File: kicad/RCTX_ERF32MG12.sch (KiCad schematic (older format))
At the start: 87 parts

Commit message: Using ERF32FG12 SoC instead of PIC32MX
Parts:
- removed C? (x2): 10u, symbol device:C
- removed C?: 10n, symbol device:C
- removed C? (x6): 1u, symbol device:C
- removed C? (x4): 100n, symbol device:C
- removed C?: 10p, symbol device:C
- removed C?: 100p, symbol device:C
- removed C?: 4u7, symbol device:C
- removed L?: BLM18AG601SN1, symbol device:L_Core_Iron
- removed L?: 4u7, symbol device:L
- removed R?: 1R, symbol device:R
- removed U?: EFR32FG12P431F1024GM68, Footprint, symbol silabs_efr32:EFR32FG12P431F1024GM68
- added C? (x2): 3p, symbol device:C
- added C?: 47u, symbol device:C
- added C?: 82u, symbol device:C
- added C? (x2): 10p, symbol device:C
- added C?: 220n, symbol device:C
- added C? (x5): 100n, symbol device:C
- added C?: 4u7, symbol device:C
- added C? (x5): 1u, symbol device:C
- added C? (x2): 10u, symbol device:C
- added C?: 10n, symbol device:C
- added C? (x3): 1n, symbol device:C
- added J?: 50 Ohm 2.4 GHz Antenna, symbol conn:Conn_Coaxial
- added L?: 150n, symbol device:L
- added L? (x2): 470n, symbol device:L
- added L? (x2): BLM18AG601SN1, symbol device:L_Core_Iron
- added L?: 4u7, symbol device:L
- added L? (x2): L, symbol device:L
- added R?: 1R, symbol device:R
- added U?: EFR32MG12P433F1024GM68, Footprint, symbol RCTX_ERF32FG12-rescue:EFR32FG12P433F1024GM68-silabs_efr32
- C?: value 1u -> 47u
- C? (x2): value 1u -> 82u
- C? (x2): value 100n -> 13p
- C?: value 100n -> 10p
- L?: value L -> 150n
- L? (x2): value L -> 180n
- L?: value L -> 390n
- L? (x2): value L -> 36n
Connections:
- wire segments 661 -> 696
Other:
- moved on the sheet: C?, J?, L?, SW?, U?, Y?

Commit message: Using ERF32FG12 SoC instead of PIC32MX
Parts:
- removed P?: ARM 20 Pin Header, symbol conn:Conn_02x10_Odd_Even
- removed P?: SWITCHES, symbol conn:Conn_02x08_Odd_Even
- added P?: SWITCHES, symbol conn:Conn_02x11_Odd_Even
- added P?: JTAG+ETM, symbol conn:Conn_02x05_Odd_Even
- U?: symbol RCTX_ERF32FG12-rescue:EFR32FG12P433F1024GM68-silabs_efr32 -> silabs_efr32:EFR32MG12P433F1024GM68
- Y?: value Si500DFAD100M000 / Si511NCB100M000C -> Si500DFAD110M000 / Si511NCB110M000C
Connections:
- net labels added: DSC, PPM_IO, PPM_TX, RF_MODE, SWCLK-TCK, SWDIO-TMS, SWO-TDO
- net labels removed: MASTER|SLAVEn, PPM_IN, PPM_OUT, RF_ENABLE, SWDCLK-TMS, SWDIO-TCK, SWDO-TDO
- wire segments 696 -> 690
- no-connect marks 12 -> 13
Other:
- moved on the sheet: C?, J?, L?, P?, U?, Y?

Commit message: Using ERF32FG12 SoC instead of PIC32MX
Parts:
- removed C? (x2): 100n, symbol device:C
- removed D? (x2): GREEN, symbol device:LED
- removed D?: D, symbol device:D
- removed D?: RED, symbol device:LED
- removed F?: Polyfuse, symbol device:Polyfuse
- removed R? (x3): 1k, symbol device:R
- removed U?: LM1117-5.0, symbol regul:LM1117-5.0
- added C? (x5): 100n, symbol device:C
- added C? (x3): 4u7, symbol device:CP
- added R?: 10k, symbol device:R
- added R?: 4k7, symbol device:R
- added U?: LM1117-3.3, symbol regul:LM1117-5.0
- added U?: LM1117-5.0, symbol regul:LM1117-5.0
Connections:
- wire segments 690 -> 695
- no-connect marks 13 -> 14
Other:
- note added: "Main power source"
- note added: "USB interface"
- note removed: "Main power source and USB interface"
- moved on the sheet: C?, J?, L?, P?, RV?, ZD?

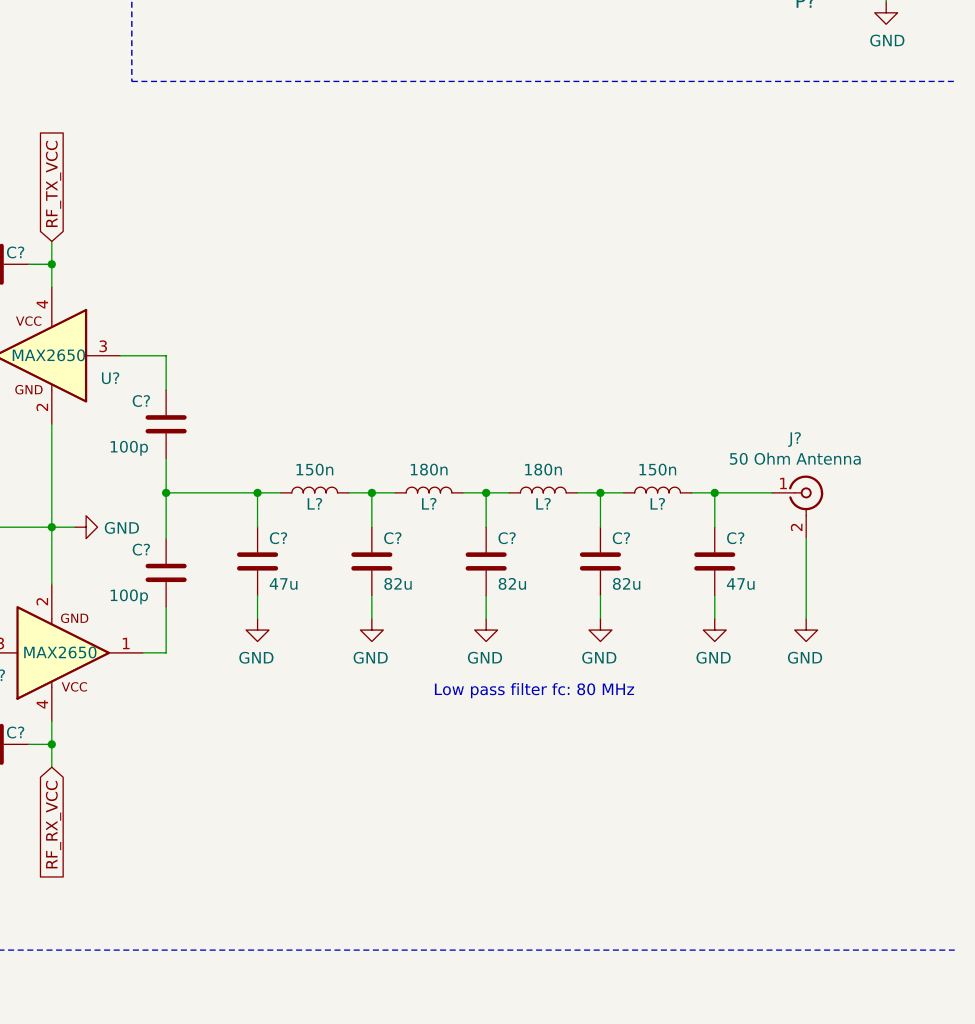
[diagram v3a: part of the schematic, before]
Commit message: Using ERF32FG12 SoC instead of PIC32MX
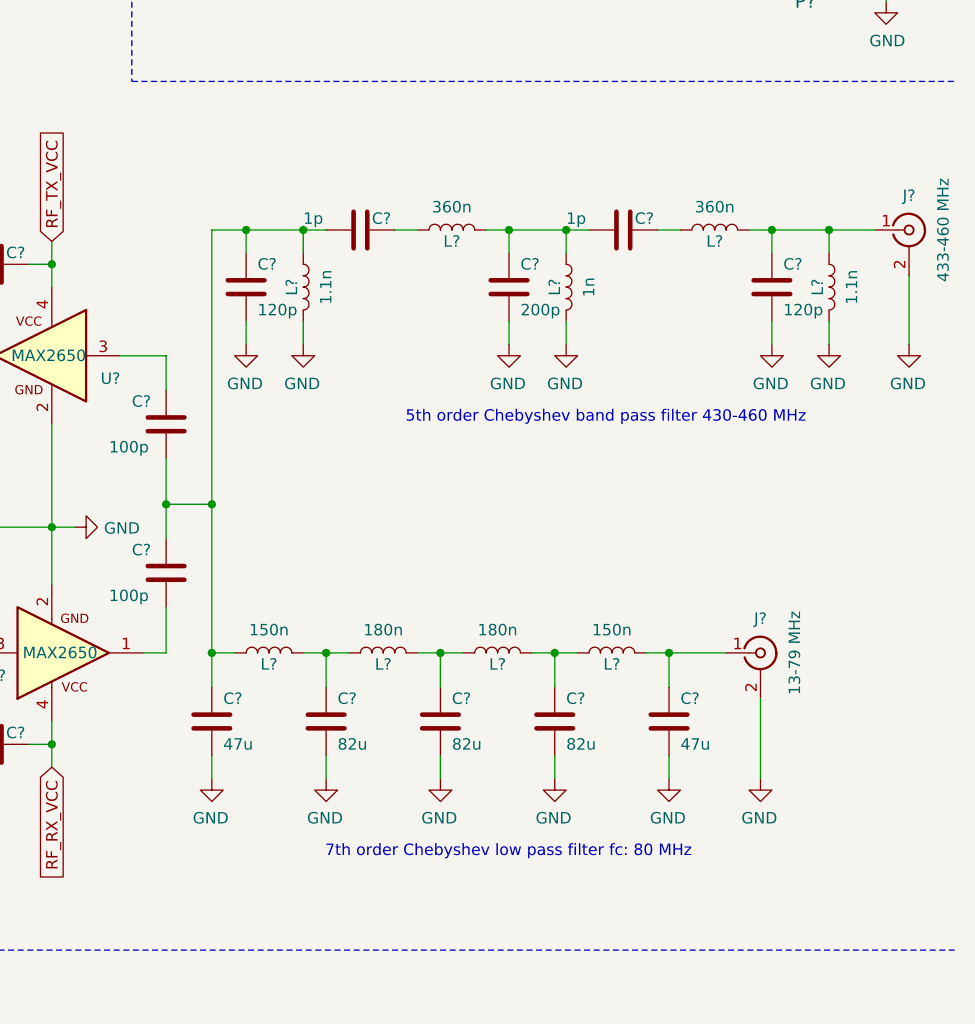
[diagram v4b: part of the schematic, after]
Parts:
- added ANT?: 433-460 MHz, symbol conn:Conn_Coaxial
- added C? (x2): 120p, symbol device:C
- added C? (x2): 1p, symbol device:C
- added C?: 200p, symbol device:C
- added L? (x2): 1.1n, symbol device:L
- added L? (x2): 360n, symbol device:L
- added L?: 1n, symbol device:L
- ANT?: renamed from J?; value 50 Ohm Antenna -> 13-79 MHz
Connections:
- wire segments 695 -> 721
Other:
- note added: "5th order Chebyshev band pass filter 430-460 MHz"
- note added: "7th order Chebyshev low pass filter fc: 80 MHz"
- note removed: "Low pass filter fc: 80 MHz"
- moved on the sheet: C?, J?, L?

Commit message: Adding wideband (110-350 MHz) matching network
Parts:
- removed C?: 3p, symbol device:C
- removed C? (x2): 1p, symbol device:C
- removed C?: 1n, symbol device:C
- removed C?: 13p, symbol device:C
- removed C?: 10p, symbol device:C
- removed L? (x2): 1.1n, symbol device:L
- removed L?: 1n, symbol device:L
- removed L?: 36n, symbol device:L
- added C? (x2): 13p, symbol device:C
- added L? (x2): 390n, symbol device:L
- added U?: JSW2-63DR+, symbol RF_Mixer:JSW2-63DR+
- C? (x2): value 47u -> 33p
- C? (x3): value 82u -> 75p
- C? (x2): value 120p -> 5.1p
- C?: value 200p -> 11p
- J?: renamed from ANT?; value 433-460 MHz -> 50 Ohm 433-460 MHz Antenna
- J?: renamed from ANT?; value 13-79 MHz -> 50 Ohm 13-79 MHz Antenna
- L? (x2): value 360n -> 22n
- L?: value 390n -> 220n
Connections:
- net labels added: RF_BAND_SEL
- wire segments 721 -> 714
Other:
- note added: "5th order Chebyshev low\npass filter 430-460 MHz"
- note removed: "5th order Chebyshev band pass filter 430-460 MHz"
- moved on the sheet: C?, J?, L?, R?, SW?, U?, Y?

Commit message: Using Pic16(L)F1459 as USB->(UART/SWD/I2C) bridge
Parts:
- removed C? (x4): 100n, symbol device:C
- removed C?: 4u7, symbol device:CP
- removed J?: USB_OTG, symbol conn:USB_OTG
- removed P?: SWITCHES, symbol conn:Conn_02x11_Odd_Even
- removed P?: JTAG+ETM, symbol conn:Conn_02x05_Odd_Even
- removed R?: 10k, symbol device:R
- removed R?: 4k7, symbol device:R
- removed U?: FT232RL, Housings_SSOP:SSOP-28_5.3x10.2mm_Pitch0.65mm, symbol ftdi:FT232RL
- added C?: 33p, symbol device:C
- added D? (x2): D, symbol device:D
- added D? (x4): 1N4148, Diodes_THT:D_5W_P5.08mm_Vertical_KathodeUp, symbol RCTX-rescue:D-device
- added HEX_SW?: RF_BAND_SEL, Buttons_Switches_THT:Nidec_Copal_SH-7010C, symbol RCTX-rescue:SW_Coded-switches
- added J?: USB_OTG, symbol conn:USB_OTG
- added P?: SWITCHES, symbol conn:Conn_02x09_Odd_Even
- added Q?: Q_PMOS_DGS, symbol device:Q_PMOS_DGS
- added R?: R, symbol device:R
- added U?: PIC16(L)F1459-I_ML, symbol PIC_USB_BRIDGE:PIC16(L)F1459-I_ML
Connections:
- net labels added: BUS_RESETn, SOC_RESETn, VBUS, VPP
- net labels removed: RESETn
- wire segments 714 -> 708
- no-connect marks 14 -> 2
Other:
- note added: "ICSPCLK / D+"
- note added: "ICSPDAT / D-"
- note added: "ICSPVDD / GND"
- note added: "ICSPVDD / VBUS"
- note added: "ICSPVPP / ID"
- moved on the sheet: C?, P?, RV?, SW?, U?, ZD?

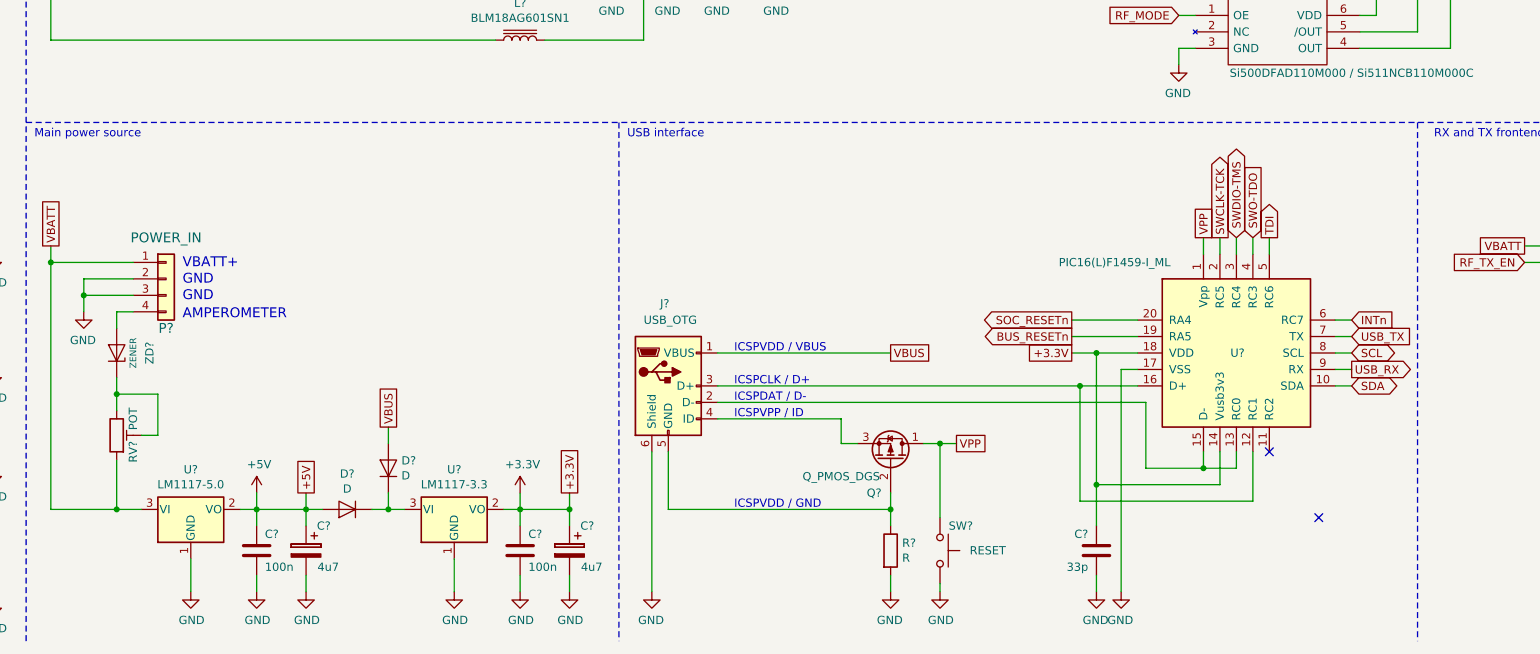
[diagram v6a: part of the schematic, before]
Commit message: Using Pic16(L)F1459 as USB->(UART/SWD/I2C) bridge
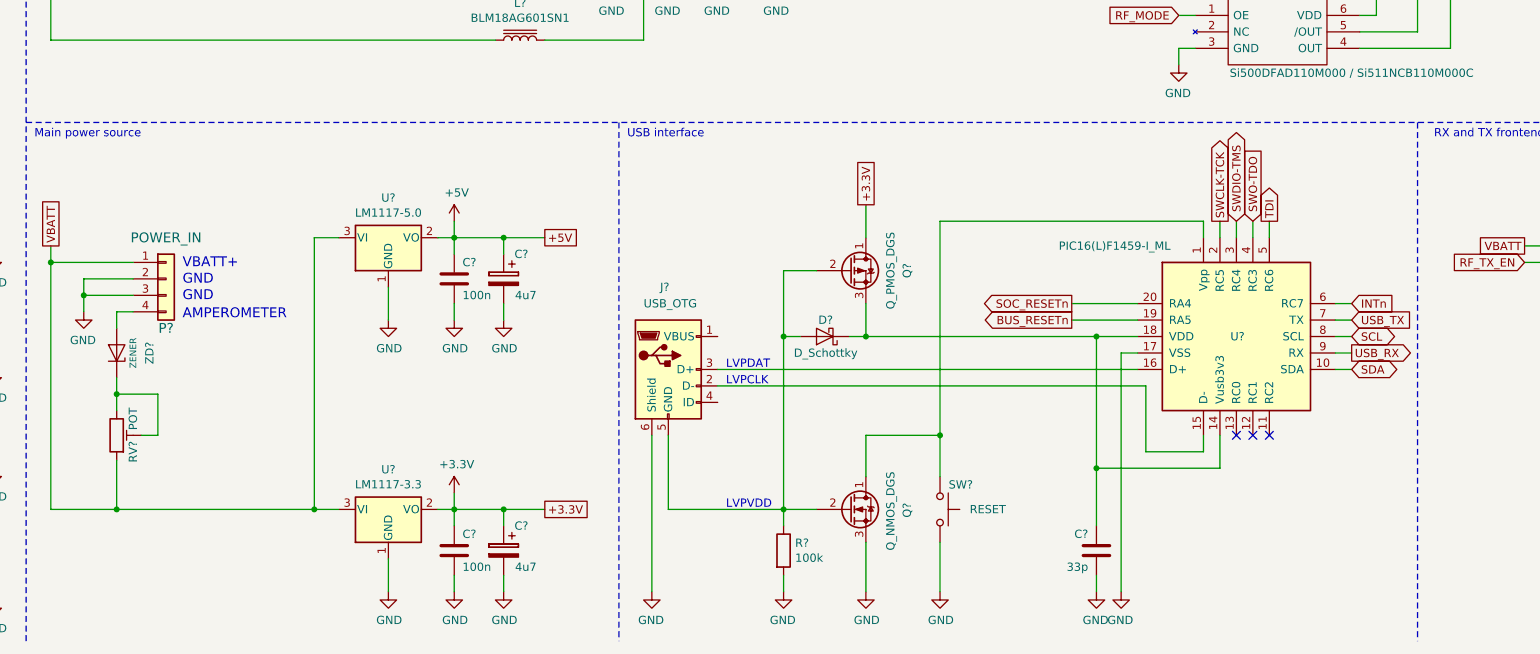
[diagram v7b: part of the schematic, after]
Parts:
- removed D? (x2): D, symbol device:D
- removed Q?: Q_PMOS_DGS, symbol device:Q_PMOS_DGS
- added D?: D_Schottky, symbol device:D_Schottky
- added Q?: Q_PMOS_DGS, symbol device:Q_PMOS_DGS
- added Q?: Q_NMOS_DGS, symbol device:Q_NMOS_DGS
- R?: value R -> 100k
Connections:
- net +3V3: now also Q?.1 (D); no longer C?.1, U?.14 (Vusb3v3), U?.18 (VDD)
- net GND: now also Q?.3 (S)
- net VBATT: now also U?.3 (VI)
- net at J?.2 (D-), U?.15 (D-): no longer U?.13 (RC0)
- net at J?.3 (D+), U?.16 (D+): no longer U?.12 (RC1)
- net at J?.5 (GND), R?.1: now also D?.2 (A), Q?.2 (G), Q?.2 (G)
- net VBUS: no longer names the net of J?.1 (VBUS)
- net VPP: no longer names the net of SW?.2, U?.1 (Vpp)
- net VPP: now also Q?.1 (D)
- new net: C?.1, D?.1 (K), Q?.3 (S), U?.14 (Vusb3v3), U?.18 (VDD)
- no-connect marks 2 -> 3
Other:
- note added: "LVPCLK"
- note added: "LVPDAT"
- note added: "LVPVDD"
- note removed: "ICSPCLK / D+"
- note removed: "ICSPDAT / D-"
- note removed: "ICSPVDD / GND"
- note removed: "ICSPVDD / VBUS"
- note removed: "ICSPVPP / ID"
- moved on the sheet: C?, J?, R?, SW?, U?

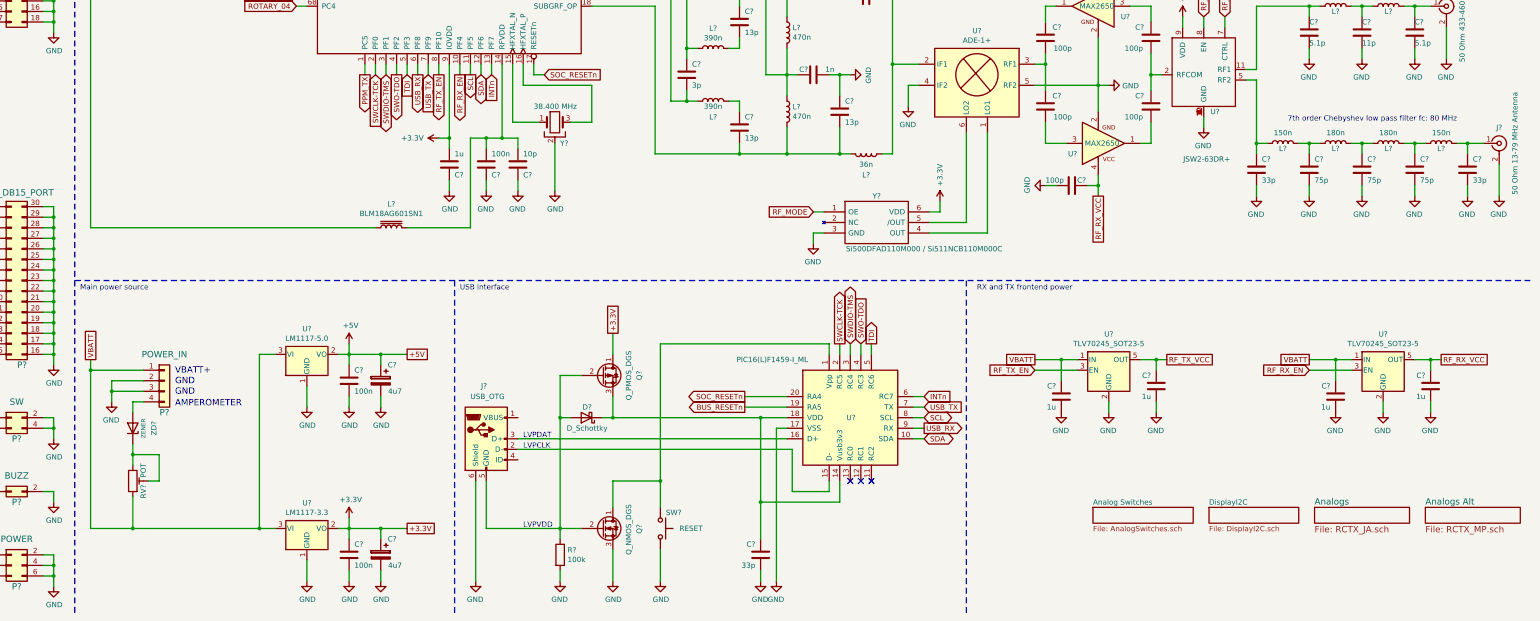
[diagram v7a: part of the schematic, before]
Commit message: Using Pic16(L)F1459 as USB->(UART/SWD/I2C) bridge
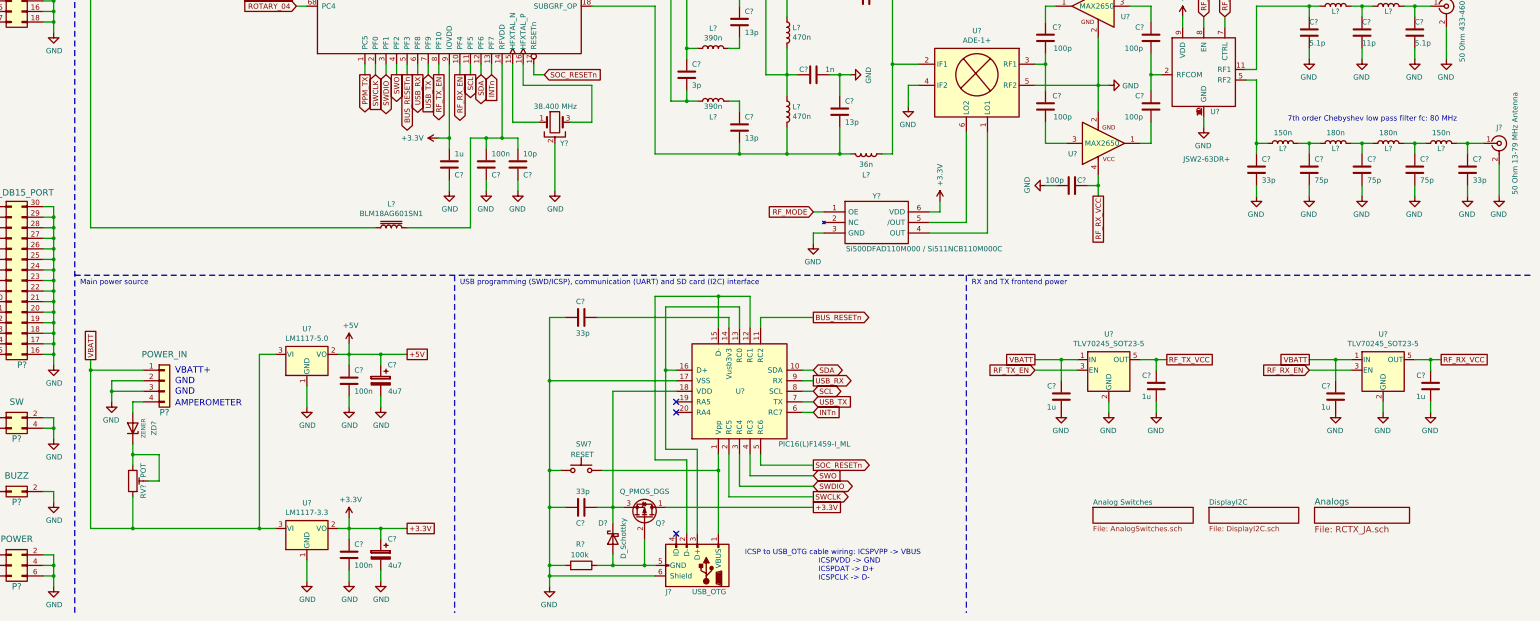
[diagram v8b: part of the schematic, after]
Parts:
- removed C?: 33p, symbol device:C
- removed D?: D_Schottky, symbol device:D_Schottky
- removed J?: USB_OTG, symbol conn:USB_OTG
- removed Q?: Q_PMOS_DGS, symbol device:Q_PMOS_DGS
- removed Q?: Q_NMOS_DGS, symbol device:Q_NMOS_DGS
- removed R?: 100k, symbol device:R
- removed SW?: RESET, symbol RCTX-rescue:SW_Push-switches
- removed U?: PIC16(L)F1459-I_ML, symbol PIC_USB_BRIDGE:PIC16(L)F1459-I_ML
- added C? (x2): 33p, symbol device:C
- added D?: D_Schottky, symbol device:D_Schottky
- added J?: USB_OTG, symbol conn:USB_OTG
- added Q?: Q_PMOS_DGS, symbol device:Q_PMOS_DGS
- added R?: 100k, symbol device:R
- added SW?: RESET, symbol RCTX-rescue:SW_Push-switches
- added U?: PIC16(L)F1459-I_ML, symbol PIC_USB_BRIDGE:PIC16(L)F1459-I_ML
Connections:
- net TDI is gone; now on net BUS_RESETn: U?.5 (PF3)
- net +3V3: now also Q?.1 (D)
- net BUS_RESETn: now also U?.11 (RC2)
- net GND: now also C?.2, C?.2, J?.6 (Shield), R?.2, SW?.2, U?.17 (VSS)
- net INTn: now also U?.6 (RC7)
- net SCL: now also U?.8 (SCL)
- net SDA: now also U?.10 (SDA)
- net SOC_RESETn: now also U?.5 (RC6)
- net USB_RX: now also U?.9 (RX)
- net USB_TX: now also U?.7 (TX)
- net SWCLK-TCK renamed SWCLK
- net SWCLK: now also U?.2 (RC5)
- net SWDIO-TMS renamed SWDIO
- net SWDIO: now also U?.3 (RC4)
- net SWO-TDO renamed SWO
- net SWO: now also U?.4 (RC3)
- new net: J?.1 (VBUS), SW?.1, U?.1 (Vpp)
- new net: J?.2 (D-), U?.12 (RC1), U?.15 (D-)
- new net: J?.3 (D+), U?.13 (RC0), U?.16 (D+)
- new net: C?.1, U?.14 (Vusb3v3)
- new net: C?.1, D?.1 (K), Q?.3 (S), U?.18 (VDD)
- new net: D?.2 (A), J?.5 (GND), Q?.2 (G), R?.1
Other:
- note added: "ICSP to USB_OTG cable wiring: ICSPVPP -> VBUS \n ICSPVDD -> GND \n ICSPDAT -> D+ \n ICSPCLK -> D-"
- note added: "USB programming (SWD/ICSP), communication (UART) and SD card (I2C) interface"
- note removed: "LVPCLK"
- note removed: "LVPDAT"
- note removed: "LVPVDD"
- note removed: "USB interface"
